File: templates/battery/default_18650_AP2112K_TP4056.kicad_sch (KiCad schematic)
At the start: 14 parts

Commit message: update sch files
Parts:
- BAT_R1, BAT_R2, BAT_R3, BAT_R4, BAT_R5: footprint ErgoCai.pretty:R_0603 -> ErgoCai.pretty:R_0603_1608Metric
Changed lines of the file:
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@@
 		(pin "3"
+		)
+		(instances
+			(project ""
+				(path "/4ad52d44-7e09-4b14-9ca9-1745a5702ae6/68034258-a593-4021-a1f0-4d7f8aae109e"
+					(reference "BAT_SW1")
+					(unit 1)
+				)
+			)
 		)
 	)
@@
 			)
 		)
-		(property "Footprint" "ErgoCai.pretty:R_0603"
+		(property "Footprint" "ErgoCai.pretty:R_0603_1608Metric"
 			(at 179.07 98.298 90)
 			(effects
@@
 		)
 		(pin "2"
+		)
+		(instances
+			(project ""
+				(path "/4ad52d44-7e09-4b14-9ca9-1745a5702ae6/68034258-a593-4021-a1f0-4d7f8aae109e"
+					(reference "BAT_R5")
+					(unit 1)
+				)
+			)
 		)
 	)
@@
 			)
 		)
-		(property "Description" ""
+		(property "Description" "Power symbol creates a global label with name \"GND\" , ground"
 			(at 224.79 93.98 0)
 			(effects
@@
 			)
 		)
-		(property "Description" ""
+		(property "Description" "Light emitting diode"
 			(at 160.02 96.52 0)
 			(effects
@@
 			)
 		)
-		(property "Description" ""
+		(property "Description" "Light emitting diode"
 			(at 160.02 87.63 0)
 			(effects
@@
 			)
 		)
-		(property "Description" ""
+		(property "Description" "Power symbol creates a global label with name \"GND\" , ground"
 			(at 106.68 102.87 0)
 			(effects
@@
 			)
 		)
-		(property "Footprint" "ErgoCai.pretty:R_0603"
+		(property "Footprint" "ErgoCai.pretty:R_0603_1608Metric"
 			(at 74.93 99.06 0)
 			(effects
@@
 			)
 		)
-		(property "Description" ""
+		(property "Description" "Resistor, small symbol"
 			(at 74.93 99.06 0)
 			(effects
@@
 		)
 		(pin "2"
+		)
+		(instances
+			(project ""
+				(path "/4ad52d44-7e09-4b14-9ca9-1745a5702ae6/68034258-a593-4021-a1f0-4d7f8aae109e"
+					(reference "BAT_R1")
+					(unit 1)
+				)
+			)
 		)
 	)
@@
 			)
 		)
-		(property "Description" ""
+		(property "Description" "Diode, small symbol"
+			(at 81.28 93.98 0)
+			(effects
+				(font
+					(size 1.27 1.27)
+				)
+				(hide yes)
+			)
+		)
+		(property "Sim.Device" "D"
+			(at 81.28 93.98 0)
+			(effects
+				(font
+					(size 1.27 1.27)
+				)
+				(hide yes)
+			)
+		)
+		(property "Sim.Pins" "1=K 2=A"
 			(at 81.28 93.98 0)
 			(effects
@@
 			)
 		)
-		(property "Description" ""
+		(property "Description" "-4.0A Id, -30V Vds, P-Channel MOSFET, SOT-23"
 			(at 86.36 85.09 0)
 			(effects
@@
 		)
 		(pin "3"
+		)
+		(instances
+			(project ""
+				(path "/4ad52d44-7e09-4b14-9ca9-1745a5702ae6/68034258-a593-4021-a1f0-4d7f8aae109e"
+					(reference "BAT_Q1")
+					(unit 1)
+				)
+			)
 		)
 	)
@@
 		(pin "5"
 		)
+		(instances
+			(project ""
+				(path "/4ad52d44-7e09-4b14-9ca9-1745a5702ae6/68034258-a593-4021-a1f0-4d7f8aae109e"
+					(reference "BAT_U1")
+					(unit 1)
+				)
+			)
+		)
 	)
 	(symbol
@@
 			)
 		)
-		(property "Description" ""
+		(property "Description" "Power symbol creates a global label with name \"GND\" , ground"
 			(at 138.43 50.8 0)
 			(effects
@@
 			)
 		)
-		(property "Footprint" "ErgoCai.pretty:R_0603"
+		(property "Footprint" "ErgoCai.pretty:R_0603_1608Metric"
 			(at 125.73 50.8 0)
 			(effects
@@
 			)
 		)
-		(property "Description" ""
+		(property "Description" "Resistor, small symbol"
 			(at 125.73 50.8 0)
 			(effects
@@
 		)
 		(pin "2"
+		)
+		(instances
+			(project ""
+				(path "/4ad52d44-7e09-4b14-9ca9-1745a5702ae6/68034258-a593-4021-a1f0-4d7f8aae109e"
+					(reference "BAT_R2")
+					(unit 1)
+				)
+			)
 		)
 	)
@@
 			)
 		)
-		(property "Description" ""
+		(property "Description" "Generic connector, single row, 01x02, script generated (kicad-library-utils/schlib/autogen/connector/)"
 			(at 83.82 50.8 0)
 			(effects
@@
 			)
 		)
-		(property "Description" ""
+		(property "Description" "Power symbol creates a global label with name \"GND\" , ground"
 			(at 74.93 101.6 0)
 			(effects
@@
 			)
 		)
-		(property "Footprint" "ErgoCai.pretty:R_0603"
+		(property "Footprint" "ErgoCai.pretty:R_0603_1608Metric"
 			(at 135.89 50.8 0)
 			(effects
@@
 			)
 		)
-		(property "Description" ""
+		(property "Description" "Resistor, small symbol"
 			(at 135.89 50.8 0)
 			(effects
@@
 		)
 		(pin "2"
+		)
+		(instances
+			(project ""
+				(path "/4ad52d44-7e09-4b14-9ca9-1745a5702ae6/68034258-a593-4021-a1f0-4d7f8aae109e"
+					(reference "BAT_R3")
+					(unit 1)
+				)
+			)
 		)
 	)
@@
 			)
 		)
-		(property "Description" ""
+		(property "Description" "Power symbol creates a global label with name \"GND\" , ground"
 			(at 91.44 45.72 0)
 			(effects
@@
 			)
 		)
-		(property "Footprint" "ErgoCai.pretty:R_0603"
+		(property "Footprint" "ErgoCai.pretty:R_0603_1608Metric"
 			(at 179.07 89.408 90)
 			(effects
@@
 		(pin "2"
 		)
-	)
+		(instances
+			(project ""
+				(path "/4ad52d44-7e09-4b14-9ca9-1745a5702ae6/68034258-a593-4021-a1f0-4d7f8aae109e"
+					(reference "BAT_R4")
+					(unit 1)
+				)
+			)
+		)
+	)

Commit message: correct footprint path, add .pretty update templates
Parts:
- removed BAT_SW1: SW_DPDT, ErgoCai.pretty:MSK-12C02, symbol jiran-ble:SW_DPDT
- added BAT_SW1: SW_DPDT_x2, ErgoCai.pretty:MSK-12C02, symbol Switch:SW_DPDT_x2
- BAT_Q1: footprint ErgoCai.pretty:SOT-23 -> Package_TO_SOT_SMD:SOT-23
- BAT_R4, BAT_R5: symbol Device:R -> Device:R_Small
- BAT_R6: footprint ErgoCai:R_0603_1608Metric -> ErgoCai.pretty:R_0603_1608Metric; symbol nrfmicro-rescue:R -> Device:R_Small
- BAT_U1: footprint ErgoCai.pretty:SOT-23-5 -> Package_TO_SOT_SMD:SOT-23-5
- BAT_U2: footprint ErgoCai.pretty:SOIC-8-1EP_3.9x4.9mm_P1.27mm_EP2.29x3mm -> Package_SO:SOIC-8-1EP_3.9x4.9mm_P1.27mm_EP2.29x3mm
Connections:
- net VBAT: now also BAT_SW1.2 (B)
- net at BAT_Q1.3 (D): now also BAT_SW1.3 (C)

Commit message: update battery module
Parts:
- BAT_Q1: footprint Package_TO_SOT_SMD:SOT-23 -> ErgoCai.pretty:SOT-23
- BAT_U1: footprint Package_TO_SOT_SMD:SOT-23-5 -> ErgoCai.pretty:SOT-23-5
- BAT_U2: footprint Package_SO:SOIC-8-1EP_3.9x4.9mm_P1.27mm_EP2.29x3mm -> ErgoCai.pretty:SOIC-8-1EP_3.9x4.9mm_P1.27mm_EP2.29x3mm

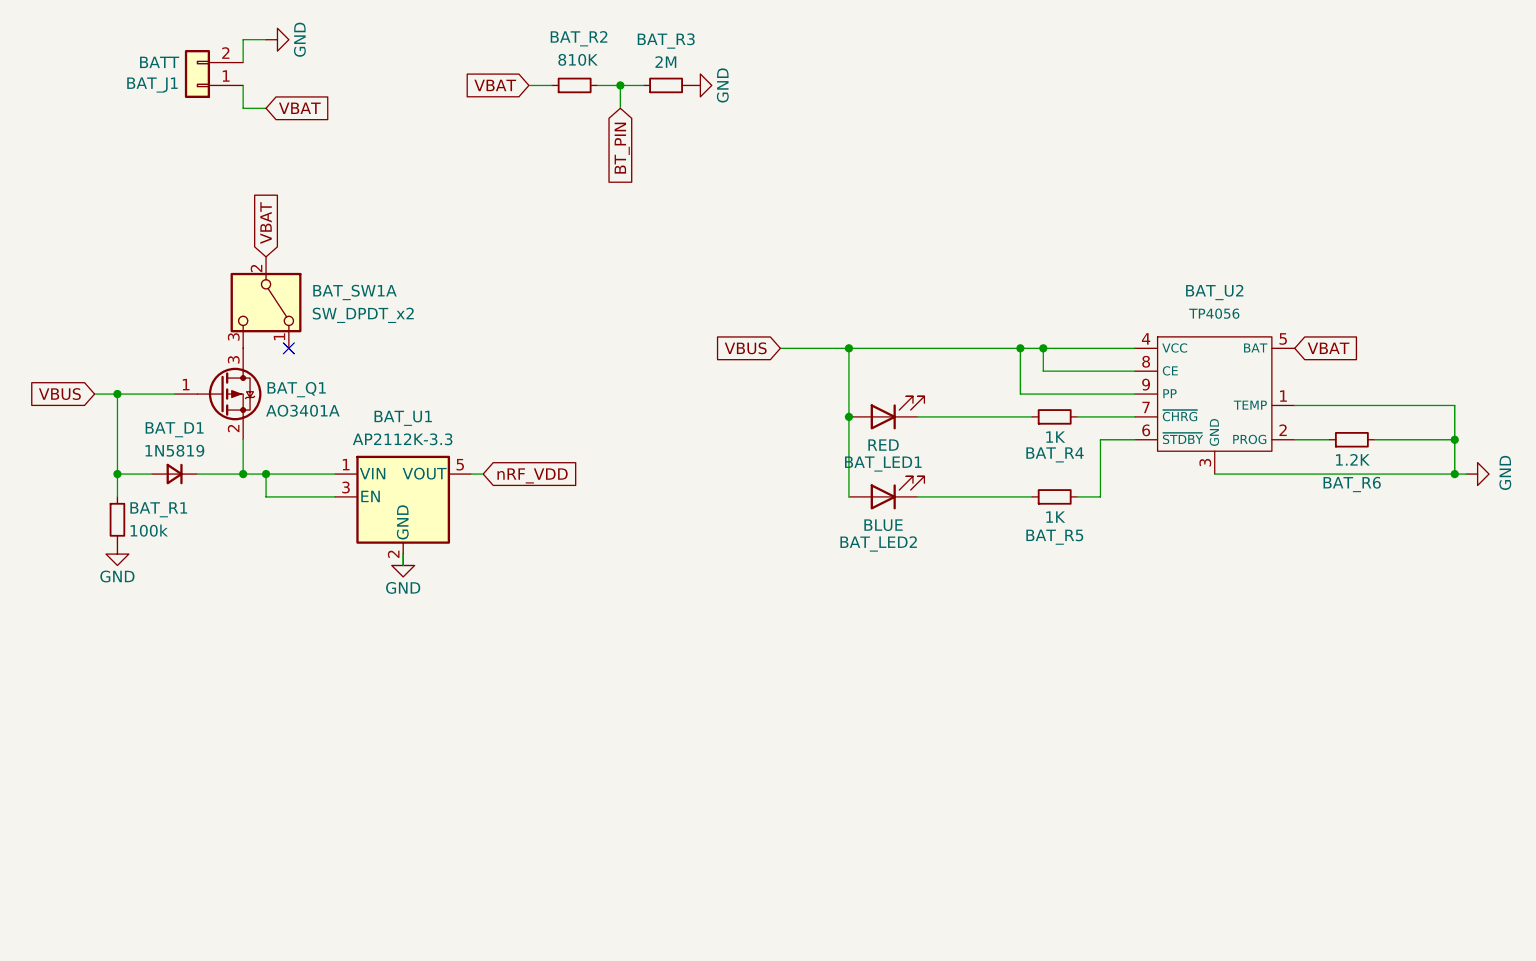
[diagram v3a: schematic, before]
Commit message: update battery U1 U2 position to ensure annotation order
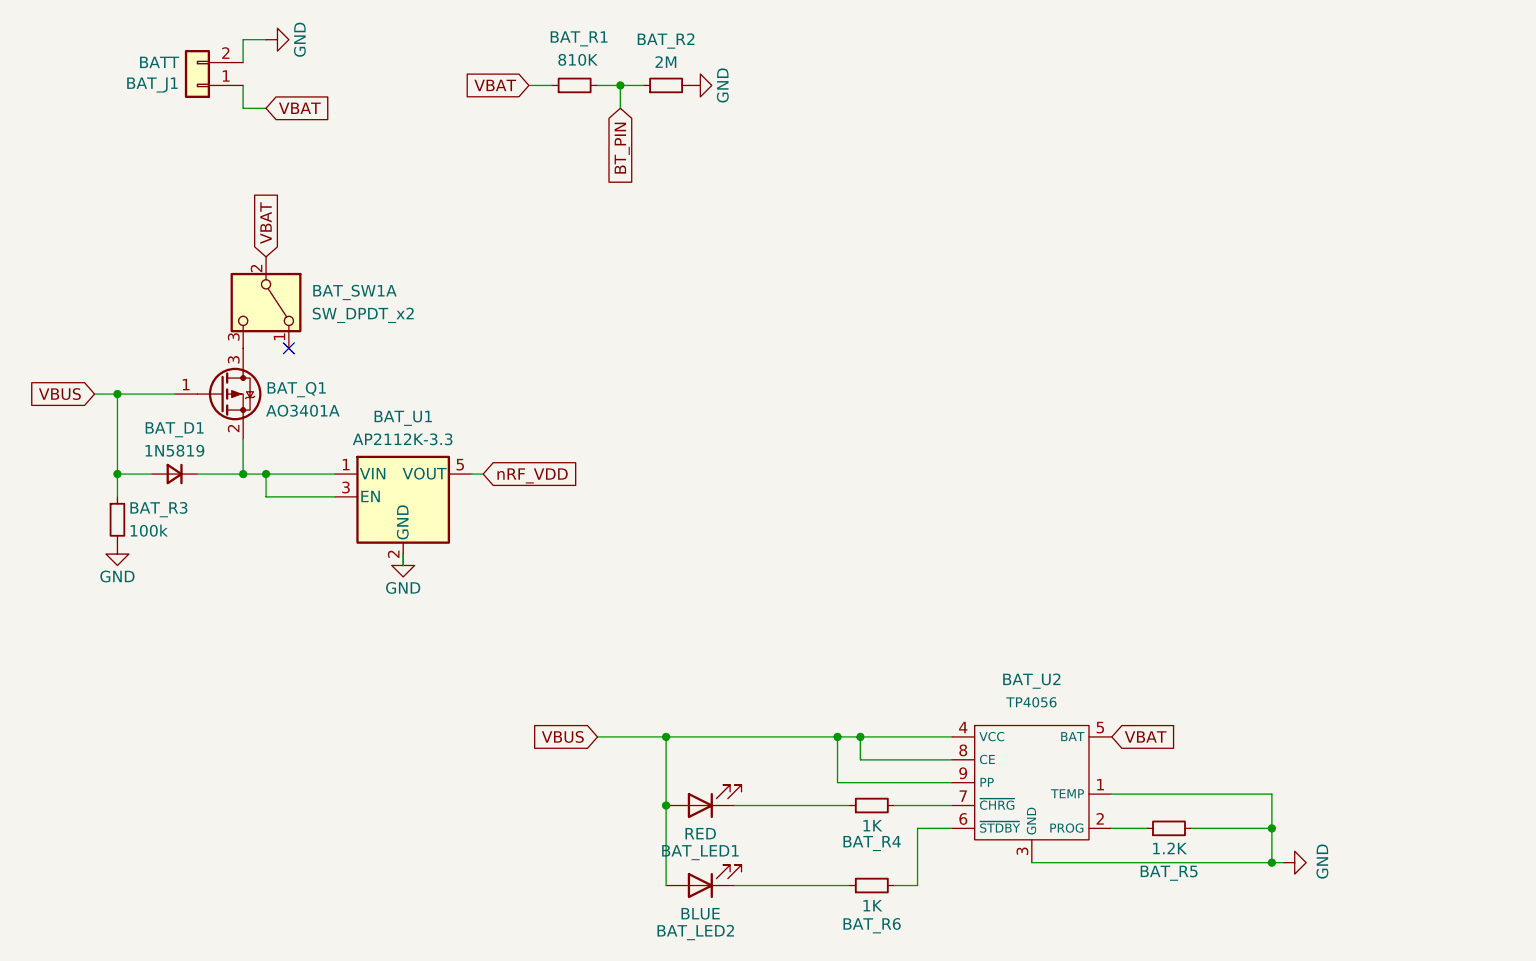
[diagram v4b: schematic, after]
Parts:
- renumbered BAT_R2 to BAT_R1, BAT_R3 to BAT_R2, BAT_R1 to BAT_R3, BAT_R6 to BAT_R5, BAT_R5 to BAT_R6
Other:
- moved on the sheet: BAT_LED1, BAT_LED2, BAT_R4, BAT_R5, BAT_R6, BAT_U2
